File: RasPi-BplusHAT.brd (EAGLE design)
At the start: 65 x 56 mm, 10 parts, among them K2 RASPI_HEADER

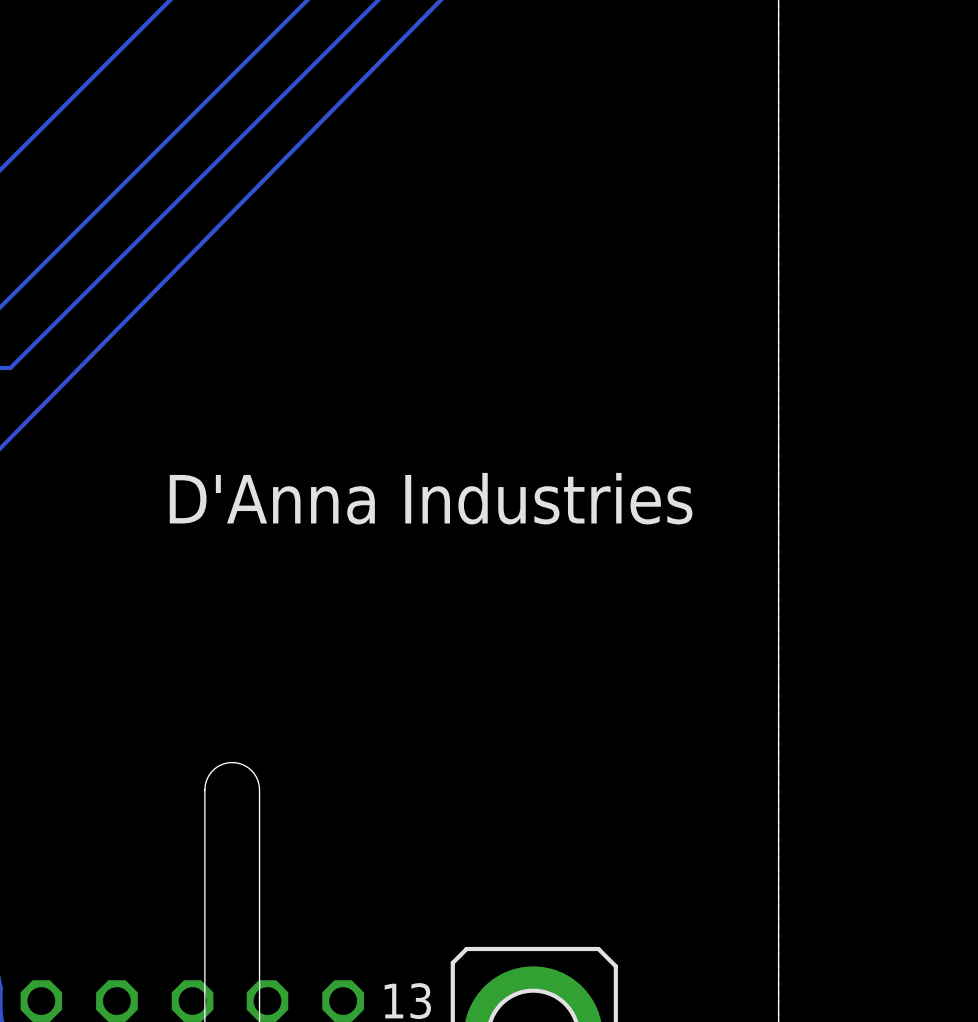
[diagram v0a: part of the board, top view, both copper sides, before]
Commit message: add level shifter
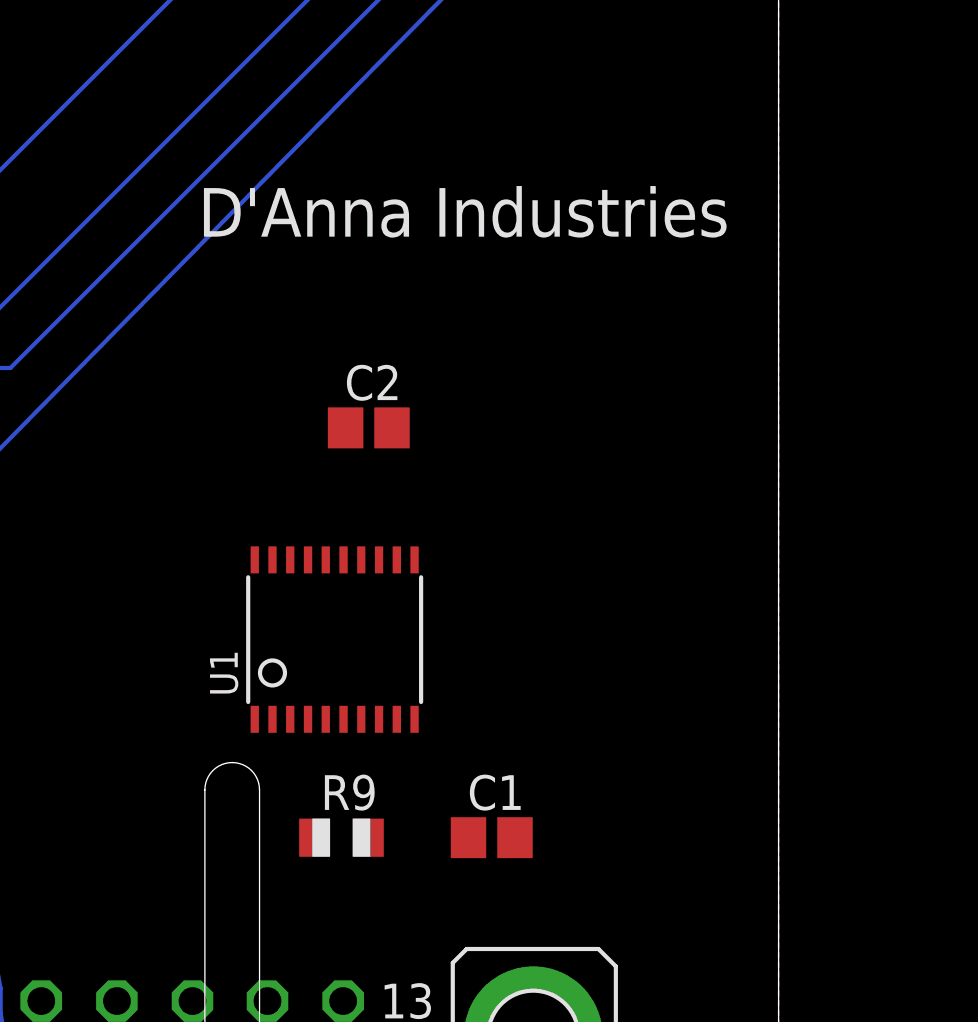
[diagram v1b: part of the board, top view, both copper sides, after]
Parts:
- added C1, C2: 0.1uF, adafruit:C0805
- added R9: 10K, adafruit:R0805
- added U1: TXB0108PWR, microbuilder:TSSOP20
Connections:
- removed net DIGI22: X1.22
- removed net DIGI23: X1.23
- removed net DIGI24: X1.24
- new net DIGIN22: U1.14, X1.22
- new net DIGIN23: U1.13, X1.23
- new net DIGIN24: U1.12, X1.24
- new net GPIO13: K2.GPIO13, U1.7
- new net GPIO17: K2.GPIO17, U1.1
- new net GPIO19: K2.GPIO19, U1.8
- new net GPIO22: K2.GPIO22, U1.4
- new net GPIO26: K2.GPIO26, U1.9
- new net GPIO27: K2.GPIO27, U1.3
- new net GPIO5: K2.GPIO5, U1.5
- new net GPIO6: K2.GPIO6, U1.6
- new net N$20: R9.1, U1.10
- net +3V3: now also C1.1, R9.2, U1.2
- net +5V: now also C2.1, U1.19
- net DIGIN10: now also U1.18
- net DIGIN11: now also U1.17
- net DIGIN12: now also U1.16
- net DIGIN13: now also U1.15
- net DIGIN9: now also U1.20
- net GND: now also C1.2, C2.2, U1.11
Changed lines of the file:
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@@
 <layer number="106" name="bPlate" color="7" fill="1" visible="yes" active="yes"/>
 <layer number="107" name="Crop" color="7" fill="1" visible="yes" active="yes"/>
+<layer number="108" name="fp8" color="7" fill="1" visible="no" active="yes"/>
+<layer number="109" name="fp9" color="7" fill="1" visible="no" active="yes"/>
+<layer number="110" name="fp0" color="7" fill="1" visible="no" active="yes"/>
 <layer number="116" name="Patch_BOT" color="7" fill="1" visible="yes" active="yes"/>
 <layer number="121" name="_tsilk" color="7" fill="1" visible="yes" active="yes"/>
 <layer number="122" name="_bsilk" color="7" fill="1" visible="yes" active="yes"/>
+<layer number="123" name="tTestmark" color="7" fill="1" visible="no" active="yes"/>
+<layer number="124" name="bTestmark" color="7" fill="1" visible="no" active="yes"/>
+<layer number="131" name="tAdjust" color="7" fill="1" visible="no" active="yes"/>
+<layer number="132" name="bAdjust" color="7" fill="1" visible="no" active="yes"/>
 <layer number="144" name="Drill_legend" color="7" fill="1" visible="yes" active="yes"/>
 <layer number="151" name="HeatSink" color="7" fill="1" visible="yes" active="yes"/>
+<layer number="199" name="Contour" color="7" fill="1" visible="yes" active="yes"/>
 <layer number="200" name="200bmp" color="7" fill="1" visible="yes" active="yes"/>
 <layer number="201" name="201bmp" color="7" fill="1" visible="yes" active="yes"/>
@@
 <layer number="207" name="207bmp" color="7" fill="1" visible="yes" active="yes"/>
 <layer number="208" name="208bmp" color="7" fill="1" visible="yes" active="yes"/>
+<layer number="209" name="209bmp" color="7" fill="1" visible="no" active="yes"/>
+<layer number="210" name="210bmp" color="7" fill="1" visible="no" active="yes"/>
 <layer number="250" name="Descript" color="7" fill="1" visible="yes" active="yes"/>
 <layer number="251" name="SMDround" color="7" fill="1" visible="yes" active="yes"/>
@@
 <wire x1="45" y1="20" x2="46" y2="19" width="0" layer="46" curve="-90"/>
 <wire x1="46" y1="19" x2="46" y2="4" width="0" layer="46"/>
-<text x="42.5" y="28.75" size="1.778" layer="21">D'Anna Industries</text>
+<text x="43.75" y="39.25" size="1.778" layer="21">D'Anna Industries</text>
 </plain>
 <attributes>
@@
 <element name="R7" library="resistor" package="0207/10" value="10k" x="30.5" y="28.5"/>
 <element name="R8" library="resistor" package="0207/10" value="10k" x="30.5" y="24.5"/>
+<element name="U1" library="microbuilder" package="TSSOP20" value="TXB0108PWR" x="48.75" y="24.5"/>
+<element name="C1" library="adafruit" package="C0805" value="0.1uF" x="54.5" y="17.25"/>
+<element name="C2" library="adafruit" package="C0805" value="0.1uF" x="50" y="32.25"/>
+<element name="R9" library="adafruit" package="R0805" value="10K" x="49" y="17.25"/>
 </elements>
 <signals>
@@
 <contactref element="K2" pad="GND@34"/>
 <contactref element="X1" pad="25"/>
+<contactref element="C1" pad="2"/>
+<contactref element="C2" pad="2"/>
+<contactref element="U1" pad="11"/>
+<wire x1="49.01" y1="53.77" x2="56.63" y2="51.23" width="0" layer="19" extent="1-1"/>
+<wire x1="43.93" y1="53.77" x2="49.01" y2="53.77" width="0" layer="19" extent="1-1"/>
+<wire x1="38.85" y1="51.23" x2="43.93" y2="53.77" width="0" layer="19" extent="1-1"/>
+<wire x1="31.23" y1="53.77" x2="38.85" y2="51.23" width="0" layer="19" extent="1-1"/>
+<wire x1="23.61" y1="53.77" x2="31.23" y2="53.77" width="0" layer="19" extent="1-1"/>
+<wire x1="18.53" y1="51.23" x2="23.61" y2="53.77" width="0" layer="19" extent="1-1"/>
+<wire x1="13.45" y1="53.77" x2="18.53" y2="51.23" width="0" layer="19" extent="1-1"/>
+<wire x1="47.6892" y1="8.73" x2="38.85" y2="51.23" width="0" layer="19" extent="1-1"/>
+<wire x1="55.35" y1="17.25" x2="47.6892" y2="8.73" width="0" layer="19" extent="1-1"/>
+<wire x1="51.675" y1="27.4178" x2="55.35" y2="17.25" width="0" layer="19" extent="1-1"/>
+<wire x1="50.85" y1="32.25" x2="51.675" y2="27.4178" width="0" layer="19" extent="1-1"/>
 </signal>
 <signal name="+3V3">
@@
 <wire x1="24.9936" y1="47.5488" x2="34.5948" y2="37.9476" width="0.1524" layer="1"/>
 <wire x1="35.052" y1="37.6428" x2="35.08" y2="37.5" width="0.1524" layer="1"/>
+<contactref element="U1" pad="2"/>
+<contactref element="R9" pad="2"/>
+<contactref element="C1" pad="1"/>
+<wire x1="50" y1="17.25" x2="53.65" y2="17.25" width="0" layer="19" extent="1-1"/>
+<wire x1="46.475" y1="21.5822" x2="50" y2="17.25" width="0" layer="19" extent="1-1"/>
+<wire x1="35.58" y1="24.5" x2="46.475" y2="21.5822" width="0" layer="19" extent="1-1"/>
 </signal>
 <signal name="+5V">
@@
 <wire x1="8.382" y1="53.7972" x2="8.37" y2="53.77" width="0.1524" layer="1"/>
 <wire x1="10.8204" y1="53.7972" x2="10.91" y2="53.77" width="0.1524" layer="1"/>
+<contactref element="C2" pad="1"/>
+<contactref element="U1" pad="19"/>
+<wire x1="46.475" y1="27.4178" x2="49.15" y2="32.25" width="0" layer="19" extent="1-1"/>
+<wire x1="10.91" y1="53.77" x2="49.15" y2="32.25" width="0" layer="19" extent="1-1"/>
 </signal>
 <signal name="ANALOG1">
@@
 <signal name="DIGIN9">
 <contactref element="X1" pad="9"/>
+<contactref element="U1" pad="20"/>
+<wire x1="38.0118" y1="11.27" x2="45.825" y2="27.4178" width="0" layer="19" extent="1-1"/>
 </signal>
 <signal name="DIGIN10">
 <contactref element="X1" pad="10"/>
+<contactref element="U1" pad="18"/>
+<wire x1="40.7804" y1="11.27" x2="47.125" y2="27.4178" width="0" layer="19" extent="1-1"/>
 </signal>
 <signal name="DIGIN12">
 <contactref element="X1" pad="12"/>
+<contactref element="U1" pad="16"/>
+<wire x1="46.2922" y1="11.27" x2="48.425" y2="27.4178" width="0" layer="19" extent="1-1"/>
 </signal>
 <signal name="DIGIN13">
 <contactref element="X1" pad="13"/>
+<contactref element="U1" pad="15"/>
+<wire x1="49.0608" y1="11.27" x2="49.075" y2="27.4178" width="0" layer="19" extent="1-1"/>
 </signal>
 <signal name="ANALOG14">
@@
 <wire x1="56.5404" y1="53.6448" x2="56.63" y2="53.77" width="0.1524" layer="16"/>
 </signal>
-<signal name="DIGI22">
-<contactref element="X1" pad="22"/>
-</signal>
-<signal name="DIGI23">
+<signal name="DIGIN23">
 <contactref element="X1" pad="23"/>
-</signal>
-<signal name="DIGI24">
+<contactref element="U1" pad="13"/>
+<wire x1="42.152" y1="8.73" x2="50.375" y2="27.4178" width="0" layer="19" extent="1-1"/>
+</signal>
+<signal name="DIGIN24">
 <contactref element="X1" pad="24"/>
+<contactref element="U1" pad="12"/>
+<wire x1="44.9206" y1="8.73" x2="51.025" y2="27.4178" width="0" layer="19" extent="1-1"/>
 </signal>
 <signal name="DIGIN11">
 <contactref element="X1" pad="11"/>
+<contactref element="U1" pad="17"/>
+<wire x1="43.549" y1="11.27" x2="47.775" y2="27.4178" width="0" layer="19" extent="1-1"/>
+</signal>
+<signal name="DIGIN22">
+<contactref element="U1" pad="14"/>
+<contactref element="X1" pad="22"/>
+<wire x1="39.4088" y1="8.73" x2="49.725" y2="27.4178" width="0" layer="19" extent="1-1"/>
+</signal>
+<signal name="GPIO27">
+<contactref element="U1" pad="3"/>
+<contactref element="K2" pad="GPIO27"/>
+<wire x1="47.125" y1="21.5822" x2="23.61" y2="51.23" width="0" layer="19" extent="1-1"/>
+</signal>
+<signal name="GPIO22">
+<contactref element="U1" pad="4"/>
+<contactref element="K2" pad="GPIO22"/>
+<wire x1="47.775" y1="21.5822" x2="26.15" y2="51.23" width="0" layer="19" extent="1-1"/>
+</signal>
+<signal name="GPIO5">
+<contactref element="U1" pad="5"/>
+<contactref element="K2" pad="GPIO5"/>
+<wire x1="48.425" y1="21.5822" x2="43.93" y2="51.23" width="0" layer="19" extent="1-1"/>
+</signal>
+<signal name="GPIO6">
+<contactref element="U1" pad="6"/>
+<contactref element="K2" pad="GPIO6"/>
+<wire x1="49.075" y1="21.5822" x2="46.47" y2="51.23" width="0" layer="19" extent="1-1"/>
+</signal>
+<signal name="GPIO13">
+<contactref element="U1" pad="7"/>
+<contactref element="K2" pad="GPIO13"/>
+<wire x1="49.725" y1="21.5822" x2="49.01" y2="51.23" width="0" layer="19" extent="1-1"/>
+</signal>
+<signal name="GPIO19">
+<contactref element="U1" pad="8"/>
+<contactref element="K2" pad="GPIO19"/>
+<wire x1="50.375" y1="21.5822" x2="51.55" y2="51.23" width="0" layer="19" extent="1-1"/>
+</signal>
+<signal name="GPIO26">
+<contactref element="U1" pad="9"/>
+<contactref element="K2" pad="GPIO26"/>
+<wire x1="51.025" y1="21.5822" x2="54.09" y2="51.23" width="0" layer="19" extent="1-1"/>
+</signal>
+<signal name="N$20">
+<contactref element="U1" pad="10"/>
+<contactref element="R9" pad="1"/>
+<wire x1="51.675" y1="21.5822" x2="48" y2="17.25" width="0" layer="19" extent="1-1"/>
+</signal>
+<signal name="GPIO17">
+<contactref element="U1" pad="1"/>
+<contactref element="K2" pad="GPIO17"/>
+<wire x1="45.825" y1="21.5822" x2="21.07" y2="51.23" width="0" layer="19" extent="1-1"/>
 </signal>
 </signals>

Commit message: re-route
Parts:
- removed C2: 0.1uF, adafruit:C0805
- added C3: .1 uF, SparkFun-Capacitors:CAP-PTH-SMALL-KIT
- C1: value 0.1uF -> .1 uF; device adafruit:C0805 -> SparkFun-Capacitors:CAP-PTH-SMALL-KIT
- R9: value 10K -> 10k; device adafruit:R0805 -> resistor:0207/10
- moved R9 24.4 mm to (56.2, 40.5), turned to 180 degrees
- moved U1 4.14 mm to (45.0, 22.8), turned to 180 degrees
- moved C1 2.93 mm to (55.5, 20.0)
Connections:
- net +3V3: now also C3.1; no longer C1.1
- net +5V: now also C1.1; no longer C2.1
- net GND: now also C3.2; no longer C2.2
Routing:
- net +5V: track 2.56 -> 79.1 mm, vias 0 -> 1
- net GPIO17: track 0.00 -> 45.6 mm, vias 0 -> 2
- net GPIO22: track 0.00 -> 43.6 mm, vias 0 -> 1
- net GPIO27: track 0.00 -> 42.1 mm, vias 0 -> 2
- net GPIO26: track 0.00 -> 37.5 mm
- net +3V3: track 77.2 -> 112.9 mm, vias 0 -> 2
- net GPIO19: track 0.00 -> 34.8 mm
- net GPIO13: track 0.00 -> 30.6 mm, vias 0 -> 1
- net GPIO6: track 0.00 -> 28.4 mm, vias 0 -> 1
- net N$20: track 0.00 -> 27.6 mm, vias 0 -> 1
- net GPIO5: track 0.00 -> 26.1 mm
- net DIGIN22: track 0.00 -> 17.9 mm
- net DIGIN24: track 0.00 -> 17.6 mm
- net DIGIN13: track 0.00 -> 15.8 mm
- net DIGIN11: track 0.00 -> 15.0 mm
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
